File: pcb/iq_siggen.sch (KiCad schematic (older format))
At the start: 94 parts, among them J1 J3 - BANK0, J10 Barrel_Jack, J11 Conn_Coaxial, J12 Conn_01x01_Male, J13 Conn_01x01_Male, J14 Conn_01x01_Male, J15 Conn_01x01_Male, J16 Conn_01x01_Male, J17 Conn_01x01_Male, J2 J4 - BANK1, J3 Conn_01x20_Male, J4 Conn_01x01_Male, J6 Conn_Coaxial, J7 Conn_Coaxial, J8 Conn_Coaxial, J9 Conn_Coaxial, SW1 SW_Push, SW2 SW_Push, U1 AMS1117-3.3, U2 TPS72325DBVR, U3 TLV73325PDBVT

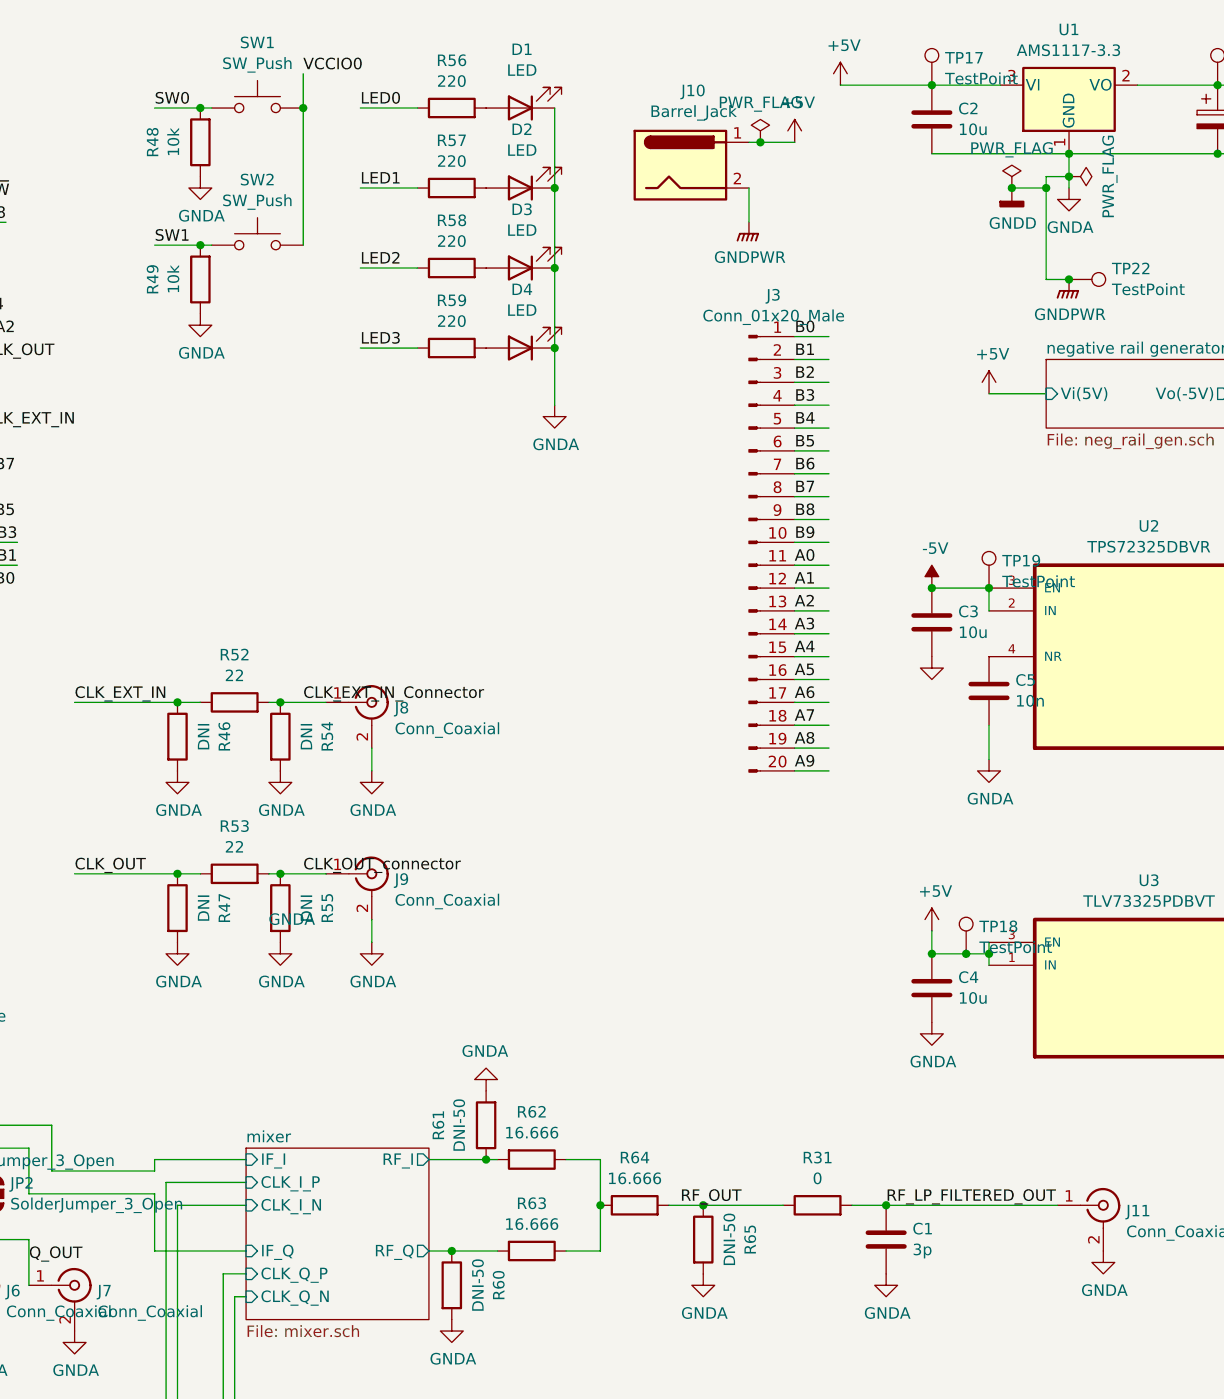
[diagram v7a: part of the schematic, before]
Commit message: populate LCSC BOM for JLCPCB assembly
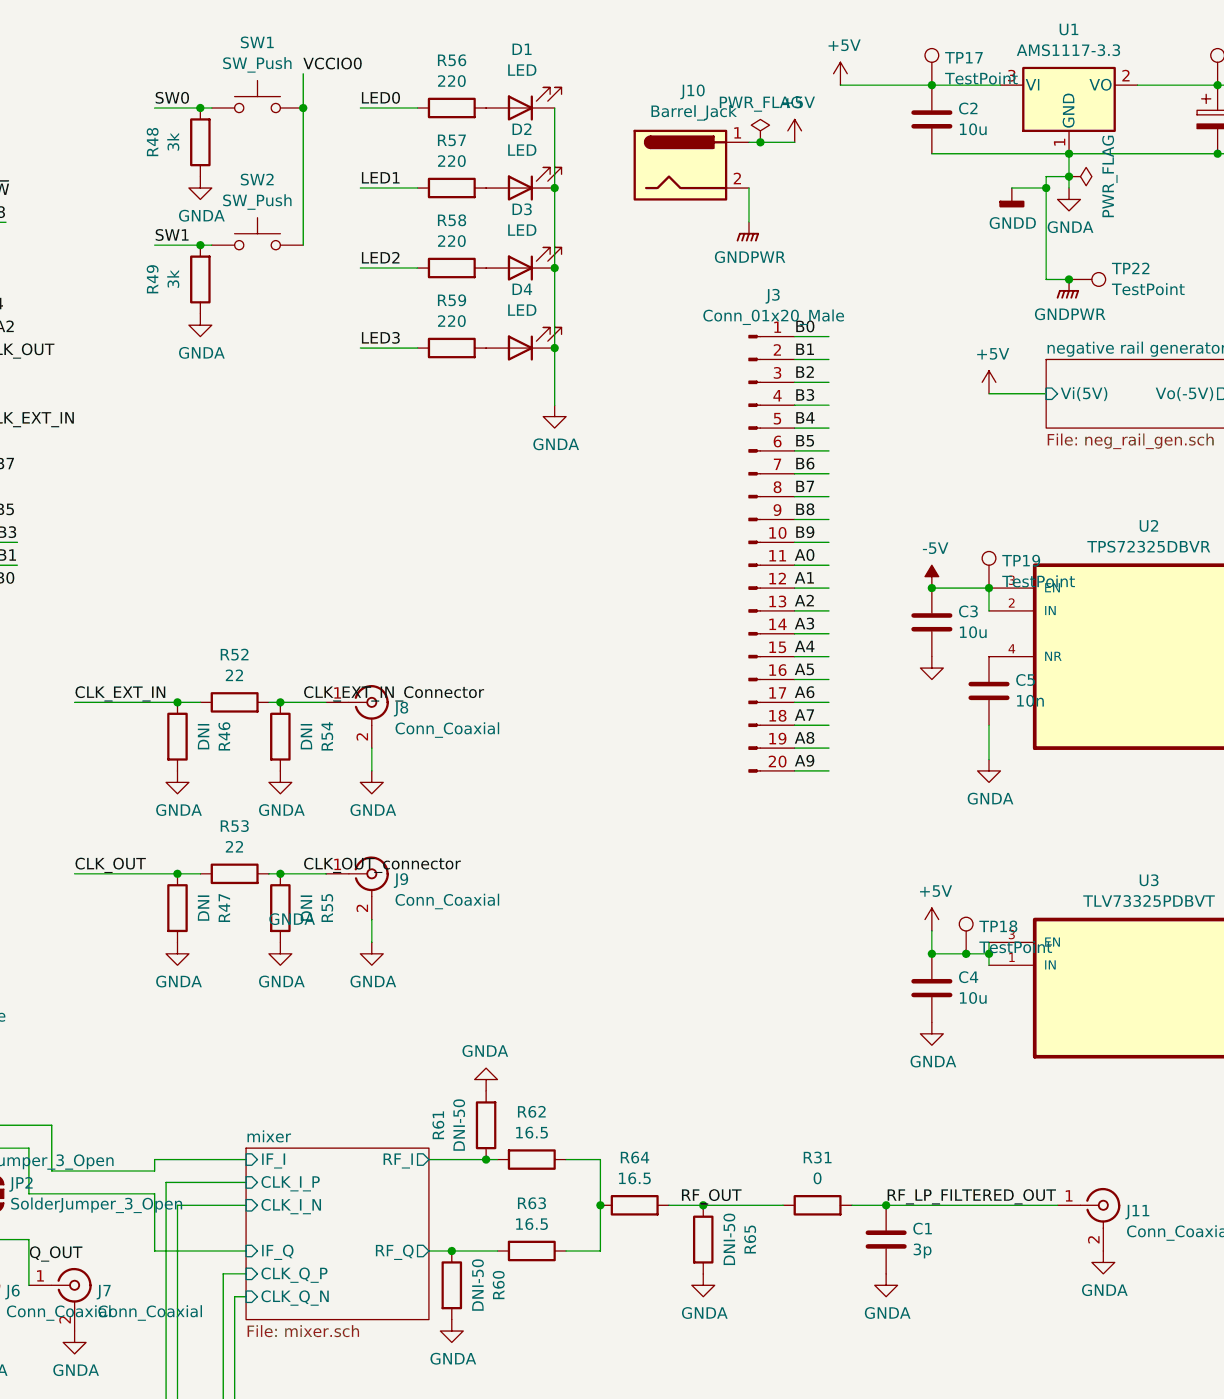
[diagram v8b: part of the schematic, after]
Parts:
- C2, C3, C4, C7, C8, C9: LCSC (none) -> C19702
- C5: LCSC (none) -> C57112
- D1, D2, D3, D4: LCSC (none) -> C34499
- R13, R14, R15, R16, R31, R6, R7: LCSC (none) -> C21189
- R17, R18, R19, R21, R22, R23, R24, R25, R26, R27, R28, R29, R34, R36, R37, R38, R39, R40, R41, R42, R43, R44, R45, R52, R53: LCSC (none) -> C23345
- R48, R49: value 10k -> 3k; LCSC (none) -> C4211
- R56, R57, R58, R59: LCSC (none) -> C22962
- R62, R63, R64: value 16.666 -> 16.5; LCSC (none) -> C12054
- R8: LCSC (none) -> C22775
- U1: LCSC (none) -> C6186
- U2: LCSC (none) -> C69932
